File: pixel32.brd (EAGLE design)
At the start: 50 x 40 mm, 129 parts, among them CON1 B7B-PH-K-S-SIDE, CON10 PINHEAD_1X01-2.54, CON11 PINHEAD_1X01-2.54, CON12 PINHEAD_1X02-2.54, CON13 PINHEAD_1X07-2, CON14 PINHEAD_1X07-2, CON2 B7B-PH-K-S-SIDE, CON3 PINHEAD_1X02-2.54, CON4 PINHEAD_1X01-2.54, CON5 PINHEAD_1X01-2.54, CON6 PINHEAD_1X01-2.54, CON7 PINHEAD_1X01-2.54, CON8 PINHEAD_1X01-2.54, CON9 PINHEAD_1X01-2.54, IC1 STM32F030K6TX-LQFP32(7X7), IC101 IRS44273L, IC201 IRS44273L, IC3 ST3485SOIC8, IC301 IRS44273L, IC6 MC74VHC1GT125, IC7 MC74VHC1GT125, IC8 LM317, Q101 N-FET-SOT23, Q201 N-FET-SOT23, Q301 N-FET-SOT23, Y1 16MHz

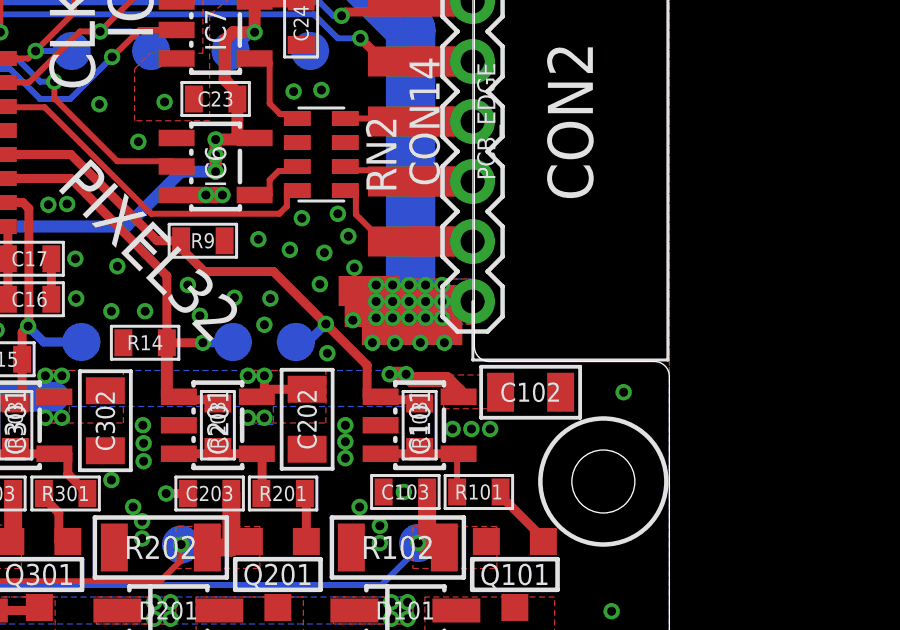
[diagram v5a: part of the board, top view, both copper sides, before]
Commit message: RTU logo removed
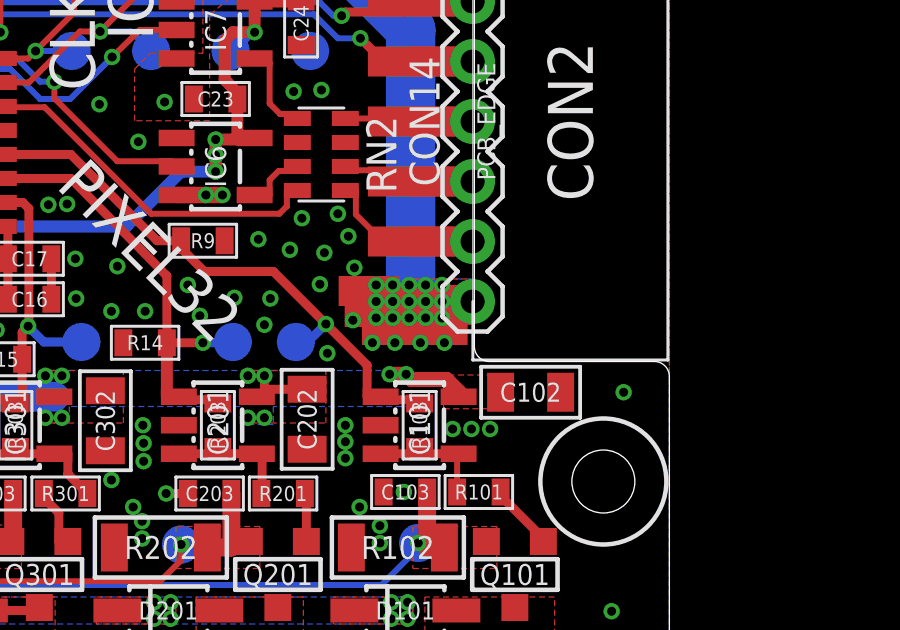
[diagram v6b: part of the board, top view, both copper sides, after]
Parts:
- removed U$1: (no value), logo:RTU
- moved U$10 0.17 mm to (17.8, 5.55)
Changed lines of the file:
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@@
 <setting verticaltext="up"/>
 </settings>
-<grid distance="1" unitdist="mm" unit="mm" style="lines" multiple="2" display="yes" altdistance="0.5" altunitdist="mm" altunit="mm"/>
+<grid distance="0.025" unitdist="mm" unit="mm" style="lines" multiple="2" display="yes" altdistance="0.5" altunitdist="mm" altunit="mm"/>
 <layers>
 <layer number="1" name="Top" color="4" fill="1" visible="yes" active="yes"/>
@@
 <attribute name="FARNELL#" value="1749366" x="-17.1" y="2.1" size="1.778" layer="27" display="off"/>
 </element>
-<element name="U$1" library="logo" package="RTU" value="" x="4.025" y="9.2" rot="MR0"/>
 <element name="CON13" library="pinhead" package="1X07-PTH-2" value="PINHEAD_1X07-2" x="-18.44" y="12" rot="R270"/>
 <element name="CON14" library="pinhead" package="1X07-PTH-2" value="PINHEAD_1X07-2" x="18.44" y="12" rot="R90"/>
@@
 <attribute name="BOM" value="EXCLUDE" x="17.25" y="5.55" size="1.778" layer="27" rot="R270" display="off"/>
 </element>
-<element name="U$10" library="usb2can_master_lib" package="CONNECTION" value="CONNECTION" x="17.6" y="5.55" rot="R270">
-<attribute name="BOM" value="EXCLUDE" x="17.6" y="5.55" size="1.778" layer="27" rot="R270" display="off"/>
+<element name="U$10" library="usb2can_master_lib" package="CONNECTION" value="CONNECTION" x="17.775" y="5.55" rot="R270">
+<attribute name="BOM" value="EXCLUDE" x="17.775" y="5.55" size="1.778" layer="27" rot="R270" display="off"/>
 </element>
 <element name="CON15" library="led_matrix_master_lib" package="B2B-PH-K-S_SIDE_MOUNT" value="" x="-18.5" y="-10.5" rot="R90"/>

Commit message: Moustashe added
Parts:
- added U$1: (no value), logo:MOUSTASHE
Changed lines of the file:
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@@
 <grid distance="0.025" unitdist="mm" unit="mm" style="lines" multiple="2" display="yes" altdistance="0.5" altunitdist="mm" altunit="mm"/>
 <layers>
-<layer number="1" name="Top" color="4" fill="1" visible="yes" active="yes"/>
+<layer number="1" name="Top" color="4" fill="1" visible="no" active="yes"/>
 <layer number="2" name="Route2" color="1" fill="3" visible="no" active="no"/>
 <layer number="3" name="Route3" color="4" fill="3" visible="no" active="no"/>
@@
 <layer number="19" name="Unrouted" color="6" fill="1" visible="yes" active="yes"/>
 <layer number="20" name="Dimension" color="15" fill="1" visible="yes" active="yes"/>
-<layer number="21" name="tPlace" color="7" fill="1" visible="yes" active="yes"/>
+<layer number="21" name="tPlace" color="7" fill="1" visible="no" active="yes"/>
 <layer number="22" name="bPlace" color="7" fill="1" visible="yes" active="yes"/>
-<layer number="23" name="tOrigins" color="15" fill="1" visible="yes" active="yes"/>
+<layer number="23" name="tOrigins" color="15" fill="1" visible="no" active="yes"/>
 <layer number="24" name="bOrigins" color="15" fill="1" visible="yes" active="yes"/>
-<layer number="25" name="tNames" color="7" fill="1" visible="yes" active="yes"/>
+<layer number="25" name="tNames" color="7" fill="1" visible="no" active="yes"/>
 <layer number="26" name="bNames" color="7" fill="1" visible="yes" active="yes"/>
 <layer number="27" name="tValues" color="7" fill="1" visible="no" active="yes"/>
@@
 <layer number="49" name="Reference" color="7" fill="1" visible="no" active="yes"/>
 <layer number="50" name="dxf" color="7" fill="1" visible="no" active="no"/>
-<layer number="51" name="tDocu" color="7" fill="1" visible="yes" active="yes"/>
+<layer number="51" name="tDocu" color="7" fill="1" visible="no" active="yes"/>
 <layer number="52" name="bDocu" color="7" fill="1" visible="yes" active="yes"/>
 <layer number="53" name="tGND_GNDA" color="7" fill="9" visible="no" active="no"/>
@@
 <attribute name="TME#" value="GRM188R71H104KA93D" x="-13.525" y="-3.775" size="1.778" layer="27" display="off"/>
 </element>
+<element name="U$1" library="logo" package="MOUSTASHE" value="" x="7.5" y="9.4" rot="MR0"/>
 </elements>
 <signals>
